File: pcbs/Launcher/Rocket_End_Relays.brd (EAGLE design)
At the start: 100 x 80 mm, 39 parts, among them IC2 LM2576T-ADJ, K4 LD105, K5 LD105, K6 LD105, K7 LD105, T1 BC547, T2 BC547, T3 BC547, T4 BC547, T5 BC547, U1 ARDUINO-MEGAPRO-5V, X2 22-23-2041, X3 22-23-2021

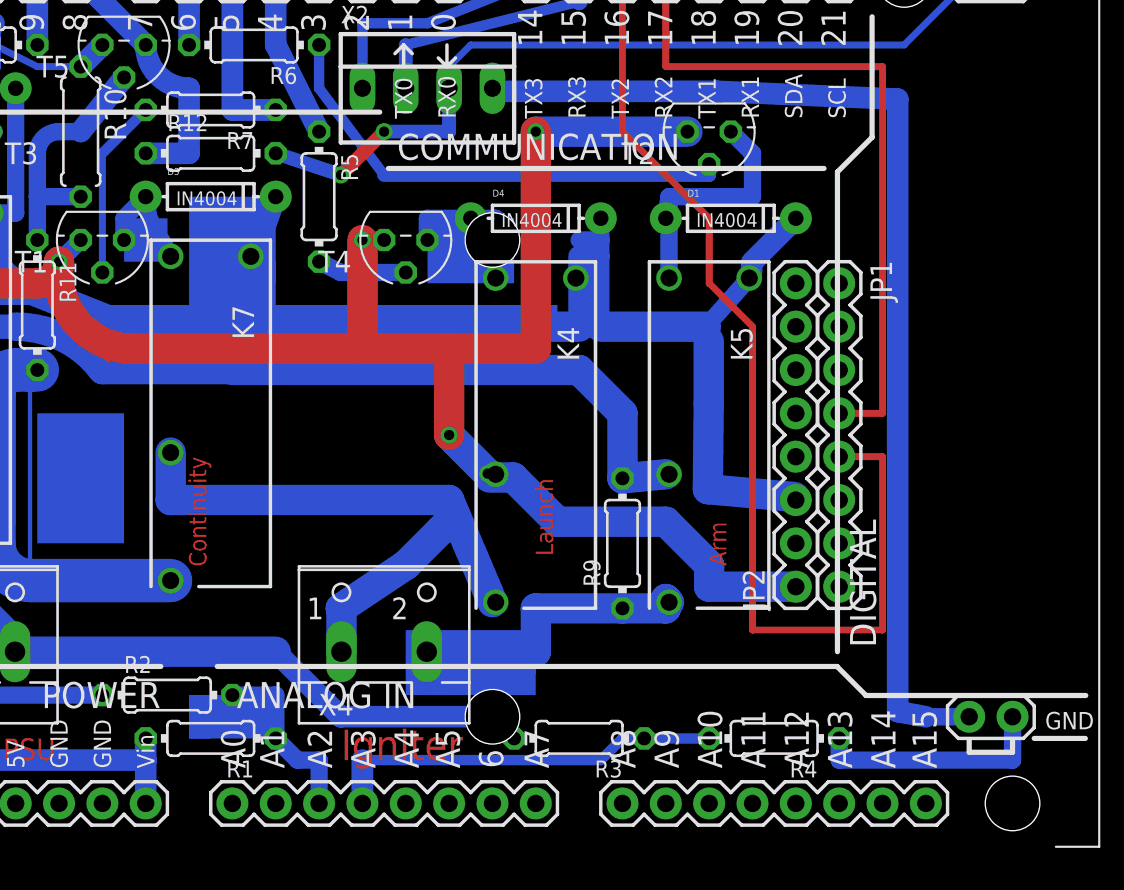
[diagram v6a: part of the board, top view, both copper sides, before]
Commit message: * Moving diode, etc out of way of RFD900+ hole
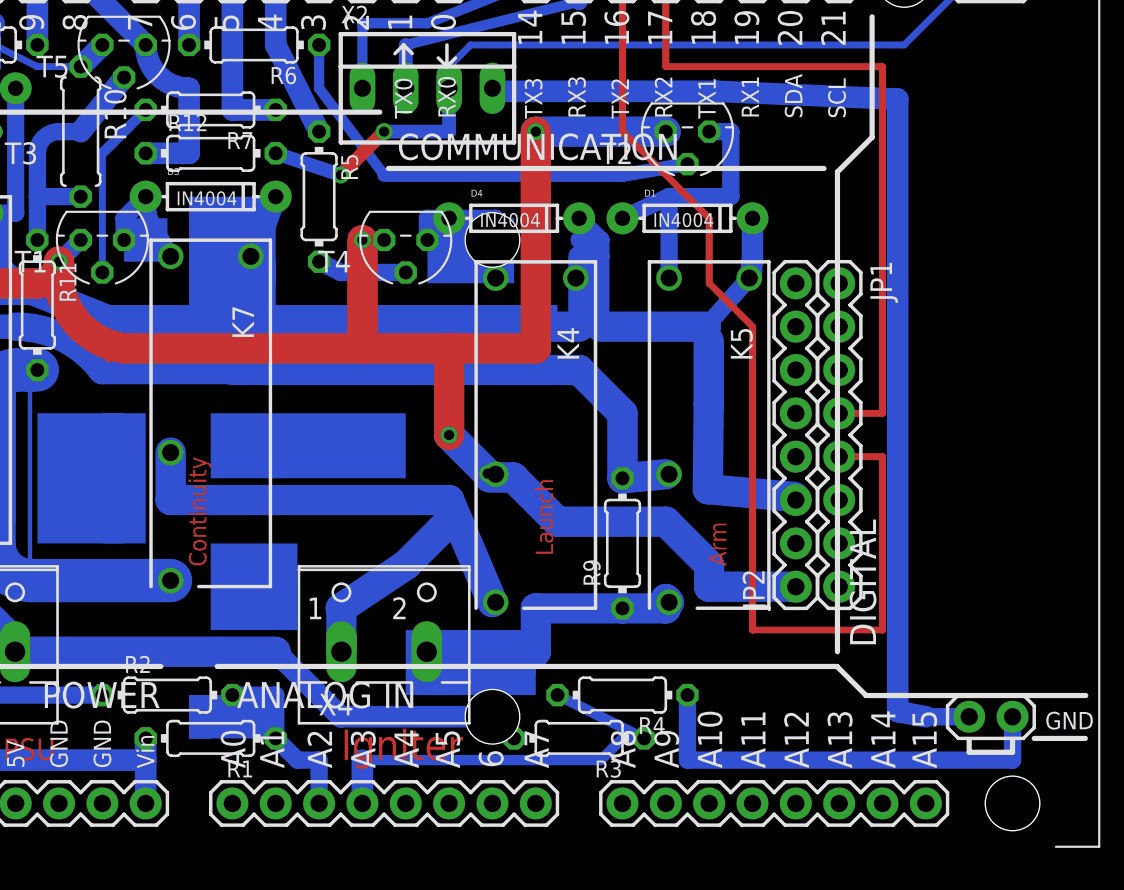
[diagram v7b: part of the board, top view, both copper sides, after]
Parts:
- moved R4 9.25 mm to (66.0, 16.5)
- moved D1 2.54 mm to (69.8, 44.5)
- moved T2 1.27 mm to (69.8, 49.5)
- moved D4 1.27 mm to (59.7, 44.5)
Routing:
- net N$24: track 14.0 -> 25.4 mm
- net N$3: track 23.4 -> 25.3 mm
- net N$10: track 28.6 -> 26.7 mm
- net N$33: track 281.8 -> 280.6 mm
- net N$22: track 15.3 -> 16.5 mm
- net N$5: track 173.7 -> 173.2 mm
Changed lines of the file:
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@@
 <rectangle x1="20.32" y1="20.32" x2="21.59" y2="34.29" layer="16"/>
 <rectangle x1="21.59" y1="20.32" x2="24.13" y2="22.86" layer="16"/>
+<rectangle x1="41.91" y1="29.21" x2="53.34" y2="33.02" layer="16"/>
+<rectangle x1="41.91" y1="20.32" x2="46.99" y2="25.4" layer="16"/>
+<rectangle x1="35.56" y1="25.4" x2="38.1" y2="33.02" layer="16"/>
 </plain>
 <attributes>
@@
 <element name="R2" library="rcl" package="0204/7" value="4.7k" x="39.37" y="16.51"/>
 <element name="R3" library="rcl" package="0204/7" value="10k" x="63.5" y="13.97" rot="R180"/>
-<element name="R4" library="rcl" package="0204/7" value="4.7k" x="74.93" y="13.97" rot="R180"/>
+<element name="R4" library="rcl" package="0204/7" value="4.7k" x="66.04" y="16.51" rot="R180"/>
 <element name="R5" library="resistor" package="0204/7" value="" x="48.26" y="45.72" rot="R270"/>
 <element name="R6" library="resistor" package="0204/7" value="1k" x="44.45" y="54.61" rot="R180"/>
@@
 <element name="R9" library="rcl" package="0204/7" value="10k" x="66.04" y="25.4" rot="R90"/>
 <element name="T1" library="transistor-neu-to92" package="TO92" value="BC547" x="35.56" y="43.18" rot="R180"/>
-<element name="T2" library="transistor-neu-to92" package="TO92" value="BC547" x="71.12" y="49.53" rot="R180"/>
+<element name="T2" library="transistor-neu-to92" package="TO92" value="BC547" x="69.85" y="49.53" rot="R180"/>
 <element name="T3" library="transistor-neu-to92" package="TO92" value="BC547" x="26.67" y="46.99"/>
 <element name="T4" library="transistor-neu-to92" package="TO92" value="BC547" x="53.34" y="43.18" rot="R180"/>
@@
 <attribute name="OC_NEWARK" value="unknown" x="41.91" y="33.02" size="0.8128" layer="27" rot="R270" display="off"/>
 </element>
-<element name="D1" library="SparkFun-DiscreteSemi" package="DIODE-1N4148" value="IN4004" x="72.39" y="44.45"/>
+<element name="D1" library="SparkFun-DiscreteSemi" package="DIODE-1N4148" value="IN4004" x="69.85" y="44.45"/>
 <element name="D2" library="SparkFun-DiscreteSemi" package="DIODE-1N4148" value="IN4004" x="26.67" y="52.07"/>
 <element name="D3" library="SparkFun-DiscreteSemi" package="DIODE-1N4148" value="IN4004" x="41.91" y="45.72"/>
-<element name="D4" library="SparkFun-DiscreteSemi" package="DIODE-1N4148" value="IN4004" x="60.96" y="44.45"/>
+<element name="D4" library="SparkFun-DiscreteSemi" package="DIODE-1N4148" value="IN4004" x="59.69" y="44.45"/>
 <element name="IC2" library="LM2576" package="TO220-5" value="LM2576T-ADJ" x="16.51" y="55.88"/>
 <element name="X3" library="con-molex" package="22-23-2021" value="22-23-2021" x="7.62" y="49.53" rot="MR270">
@@
 <contactref element="R3" pad="1"/>
 <contactref element="R4" pad="2"/>
-<wire x1="67.31" y1="13.97" x2="71.12" y2="13.97" width="0.6096" layer="16"/>
+<wire x1="67.31" y1="13.97" x2="62.23" y2="16.51" width="0.6096" layer="16"/>
 <wire x1="67.31" y1="13.97" x2="66.04" y2="13.97" width="0.6096" layer="16"/>
 <wire x1="66.04" y1="13.97" x2="64.77" y2="12.7" width="0.6096" layer="16"/>
@@
 <wire x1="48.26" y1="54.61" x2="48.26" y2="52.07" width="0.6096" layer="16"/>
 <wire x1="48.26" y1="52.07" x2="52.07" y2="46.99" width="0.6096" layer="16"/>
-<wire x1="52.07" y1="46.99" x2="71.12" y2="46.99" width="0.8128" layer="16"/>
-<wire x1="71.12" y1="47.625" x2="71.12" y2="46.99" width="0.8128" layer="16"/>
+<wire x1="52.07" y1="46.99" x2="66.04" y2="46.99" width="0.8128" layer="16"/>
+<wire x1="69.85" y1="47.625" x2="66.04" y2="46.99" width="0.8128" layer="16"/>
 </signal>
 <signal name="N$11">
@@
 <contactref element="K4" pad="2"/>
 <contactref element="D4" pad="A"/>
-<wire x1="57.15" y1="44.45" x2="58.61" y2="44.45" width="1.016" layer="16"/>
+<wire x1="55.88" y1="44.45" x2="58.61" y2="44.45" width="1.016" layer="16"/>
 <wire x1="58.61" y1="44.45" x2="58.61" y2="40.95" width="1.016" layer="16"/>
 <wire x1="54.61" y1="43.18" x2="54.61" y2="44.45" width="1.016" layer="16"/>
-<wire x1="54.61" y1="44.45" x2="57.15" y2="44.45" width="1.016" layer="16"/>
+<wire x1="54.61" y1="44.45" x2="55.88" y2="44.45" width="1.016" layer="16"/>
 </signal>
 <signal name="N$20">
@@
 <contactref element="D1" pad="A"/>
 <wire x1="68.77" y1="45.72" x2="68.77" y2="40.95" width="1.016" layer="16"/>
-<wire x1="68.58" y1="44.45" x2="68.77" y2="45.72" width="1.016" layer="16"/>
-<wire x1="68.77" y1="45.72" x2="73.66" y2="45.72" width="1.016" layer="16"/>
-<wire x1="73.66" y1="45.72" x2="73.66" y2="48.26" width="1.016" layer="16"/>
-<wire x1="73.66" y1="48.26" x2="72.39" y2="49.53" width="1.016" layer="16"/>
+<wire x1="66.04" y1="44.45" x2="68.77" y2="45.72" width="1.016" layer="16"/>
+<wire x1="68.77" y1="45.72" x2="72.39" y2="45.72" width="1.016" layer="16"/>
+<wire x1="72.39" y1="45.72" x2="72.39" y2="49.53" width="1.016" layer="16"/>
+<wire x1="72.39" y1="49.53" x2="71.12" y2="49.53" width="1.016" layer="16"/>
 </signal>
 <signal name="N$26">
@@
 <wire x1="63.5" y1="42.22" x2="64.77" y2="42.22" width="1.016" layer="16"/>
 <wire x1="64.77" y1="42.22" x2="64.77" y2="43.18" width="1.016" layer="16"/>
-<wire x1="64.77" y1="44.45" x2="64.77" y2="43.18" width="1.016" layer="16"/>
+<wire x1="63.5" y1="44.45" x2="64.77" y2="43.18" width="1.016" layer="16"/>
 <wire x1="64.77" y1="42.22" x2="64.77" y2="38.1" width="1.016" layer="16"/>
 <wire x1="64.77" y1="38.1" x2="70.93" y2="38.1" width="1.778" layer="16"/>
@@
 <wire x1="29.0322" y1="44.8056" x2="29.02" y2="44.76" width="0.254" layer="16"/>
 <wire x1="29.0322" y1="44.8056" x2="29.21" y2="44.45" width="0.254" layer="16"/>
-<wire x1="73.66" y1="41.91" x2="76.2" y2="44.45" width="1.27" layer="16"/>
+<wire x1="73.66" y1="41.91" x2="73.66" y2="44.45" width="1.27" layer="16"/>
 <wire x1="71.5264" y1="37.719" x2="70.93" y2="38.1" width="0.254" layer="16"/>
 <wire x1="73.6092" y1="41.3766" x2="73.6092" y2="41.8338" width="1.27" layer="16"/>
@@
 <contactref element="U1" pad="GND@3"/>
 <wire x1="88.9" y1="15.24" x2="88.9" y2="12.7" width="1.016" layer="16"/>
-<wire x1="88.9" y1="12.7" x2="78.74" y2="12.7" width="1.016" layer="16"/>
-<wire x1="78.74" y1="12.7" x2="78.74" y2="13.97" width="1.016" layer="16"/>
+<wire x1="88.9" y1="12.7" x2="69.85" y2="12.7" width="1.016" layer="16"/>
+<wire x1="69.85" y1="12.7" x2="69.85" y2="16.51" width="1.016" layer="16"/>
 </signal>
 <signal name="N$37">
@@
 <wire x1="55.88" y1="36.83" x2="60.96" y2="36.83" width="1.778" layer="1"/>
 <wire x1="60.96" y1="36.83" x2="60.96" y2="49.53" width="1.778" layer="1"/>
-<wire x1="60.96" y1="49.53" x2="69.85" y2="49.53" width="1.778" layer="16"/>
+<wire x1="60.96" y1="49.53" x2="68.58" y2="49.53" width="1.778" layer="16"/>
 <via x="29.21" y="49.53" extent="1-16" drill="0.6" shape="square"/>
 <via x="33.02" y="41.91" extent="1-16" drill="0.6" shape="square"/>

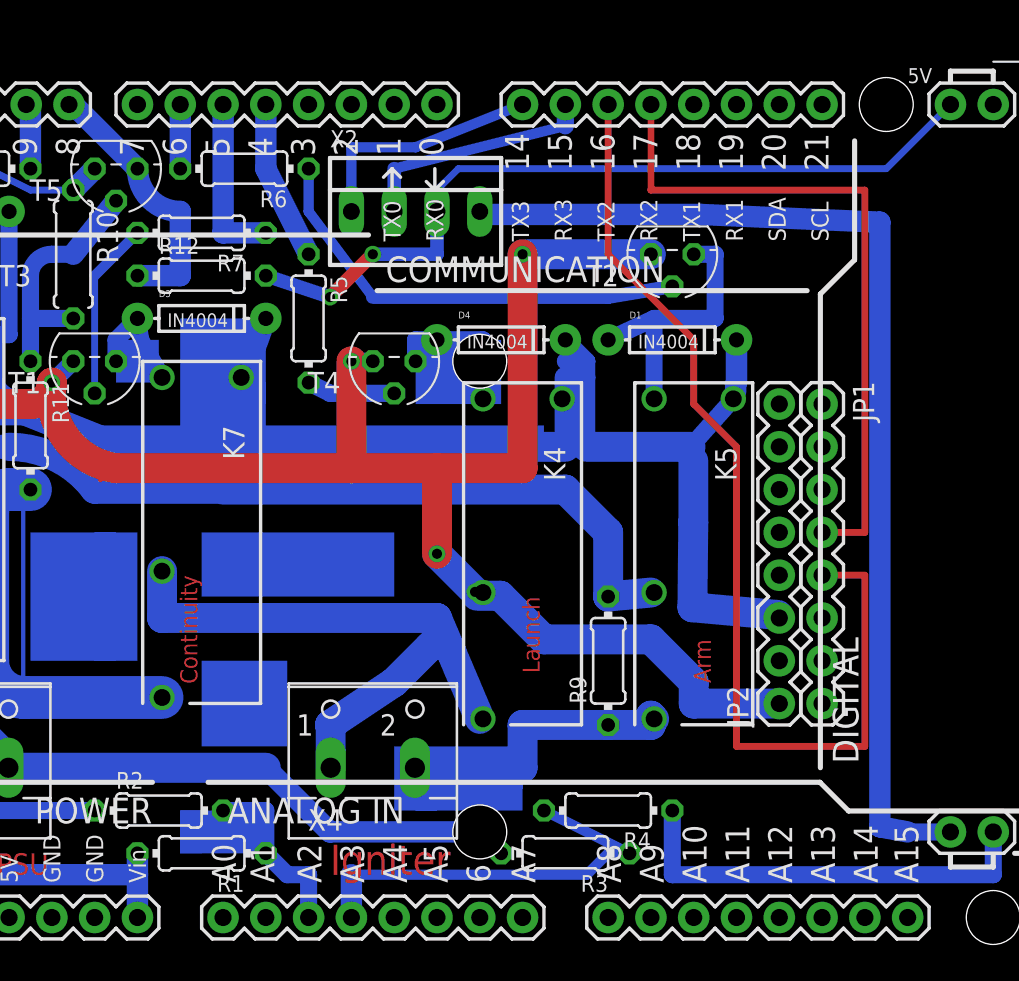
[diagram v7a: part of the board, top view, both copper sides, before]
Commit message: * Moved track from where holes are. * moved holes for rfd900 header back a bit to allow gap between it and the relay.
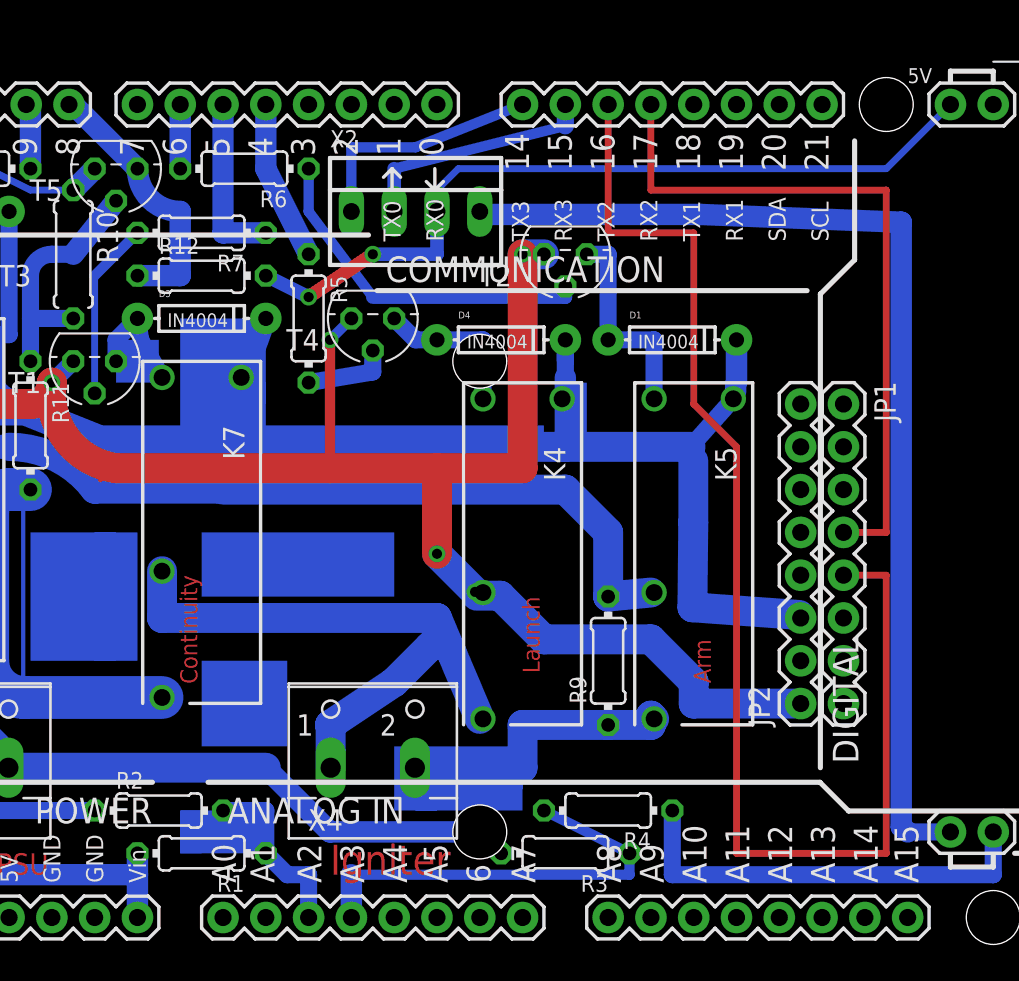
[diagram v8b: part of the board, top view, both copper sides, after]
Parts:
- moved T2 6.35 mm to (63.5, 49.5)
- moved T4 2.84 mm to (52.1, 45.7)
- moved JP1 1.27 mm to (80.0, 40.6)
- moved JP2 1.27 mm to (77.5, 22.9)
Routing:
- net N$1: track 61.6 -> 78.5 mm
- net N$10: track 26.7 -> 21.0 mm
- net N$5: track 173.2 -> 168.6 mm
- net N$22: track 16.5 -> 12.6 mm
- net N$33: track 280.6 -> 277.3 mm
- net N$2: track 40.6 -> 41.9 mm
- net N$3: track 25.3 -> 26.0 mm
- net N$19: track 8.77 -> 9.30 mm
